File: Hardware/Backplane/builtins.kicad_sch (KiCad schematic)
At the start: 37 parts, among them J1003 BM04B-SRSS-TB, J1004 BM04B-SRSS-TB, J1005 BM04B-SRSS-TB, J1006 BM04B-SRSS-TB, Q1004 S3134K, Q1005 S3134K, SW1001 Button 12mm, U1003 CD74HC221M96, U1004 PCF8523T/1,118, Y1001 32.768k

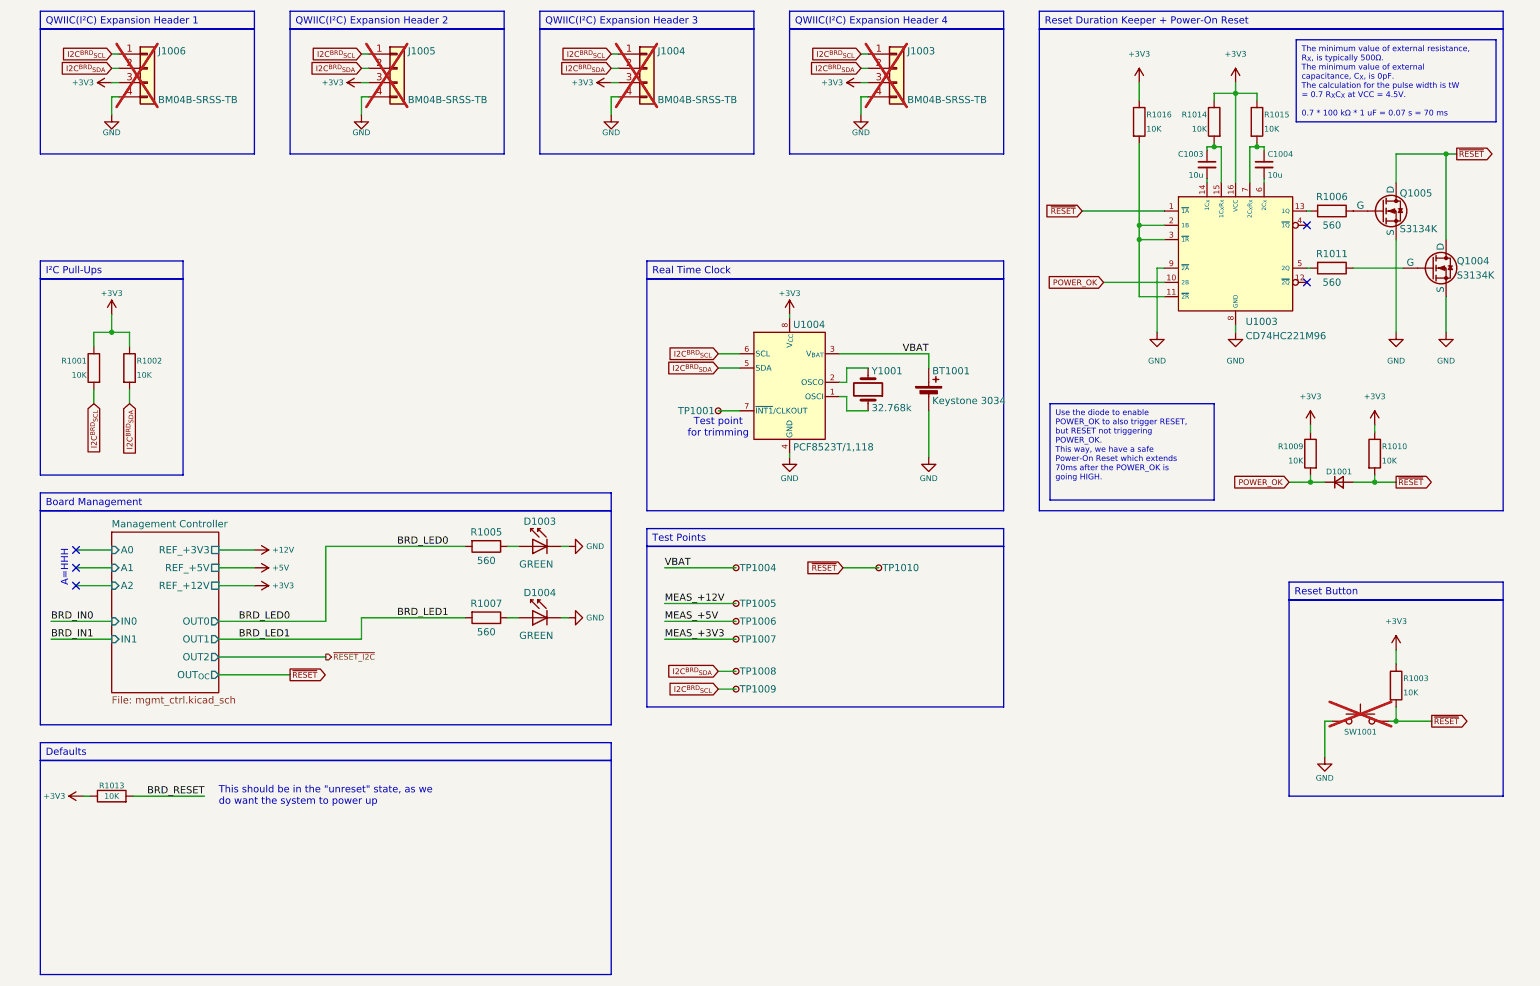
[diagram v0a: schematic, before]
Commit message: Fixes several issues with the backplane schematic.
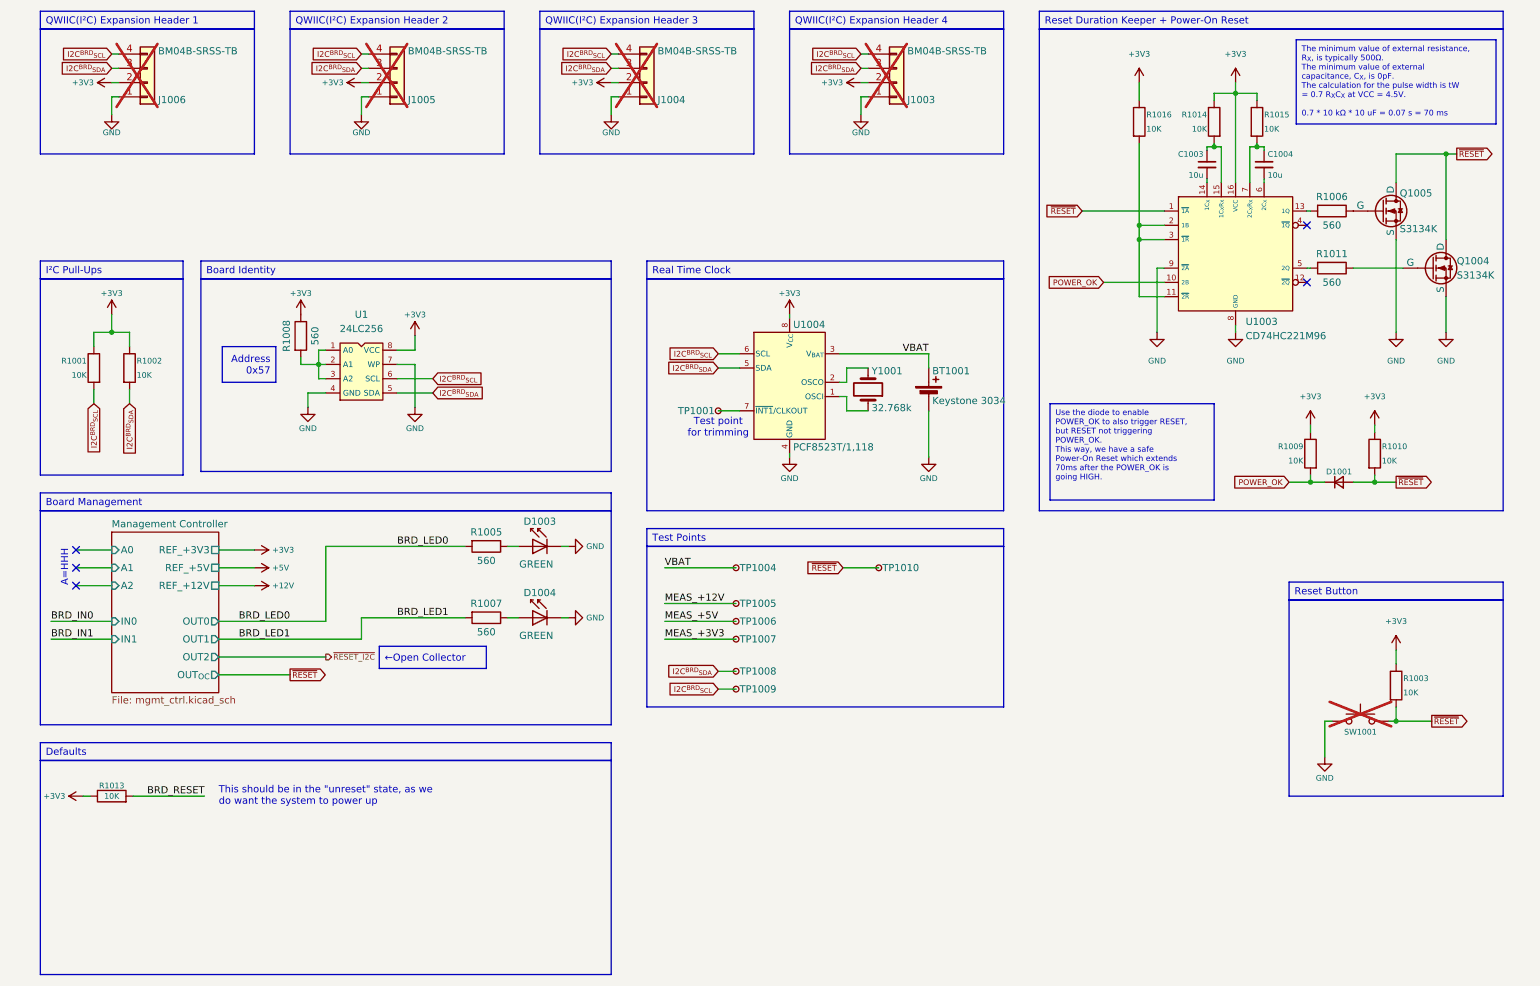
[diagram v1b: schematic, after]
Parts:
- added R1008: 560, Resistor_SMD:R_0603_1608Metric, symbol Device:R
- added U1: 24LC256, Package_SO:SOIC-8_3.9x4.9mm_P1.27mm, symbol Home Computer:24LC256
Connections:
- net +3V3: now also J1003.2 (Pin_2), J1004.2 (Pin_2), J1005.2 (Pin_2), J1006.2 (Pin_2), R1008.1, U1.8 (VCC); no longer J1003.3 (Pin_3), J1004.3 (Pin_3), J1005.3 (Pin_3), J1006.3 (Pin_3)
- net GND: now also J1003.1 (Pin_1), J1004.1 (Pin_1), J1005.1 (Pin_1), J1006.1 (Pin_1), U1.4 (GND), U1.7 (WP); no longer J1003.4 (Pin_4), J1004.4 (Pin_4), J1005.4 (Pin_4), J1006.4 (Pin_4)
- net I2C^{BRD}_{SCL}: now also J1003.4 (Pin_4), J1004.4 (Pin_4), J1005.4 (Pin_4), J1006.4 (Pin_4), U1.6 (SCL); no longer J1003.1 (Pin_1), J1004.1 (Pin_1), J1005.1 (Pin_1), J1006.1 (Pin_1)
- net I2C^{BRD}_{SDA}: now also J1003.3 (Pin_3), J1004.3 (Pin_3), J1005.3 (Pin_3), J1006.3 (Pin_3), U1.5 (SDA); no longer J1003.2 (Pin_2), J1004.2 (Pin_2), J1005.2 (Pin_2), J1006.2 (Pin_2)
- new net: R1008.2, U1.1 (A0), U1.2 (A1), U1.3 (A2)

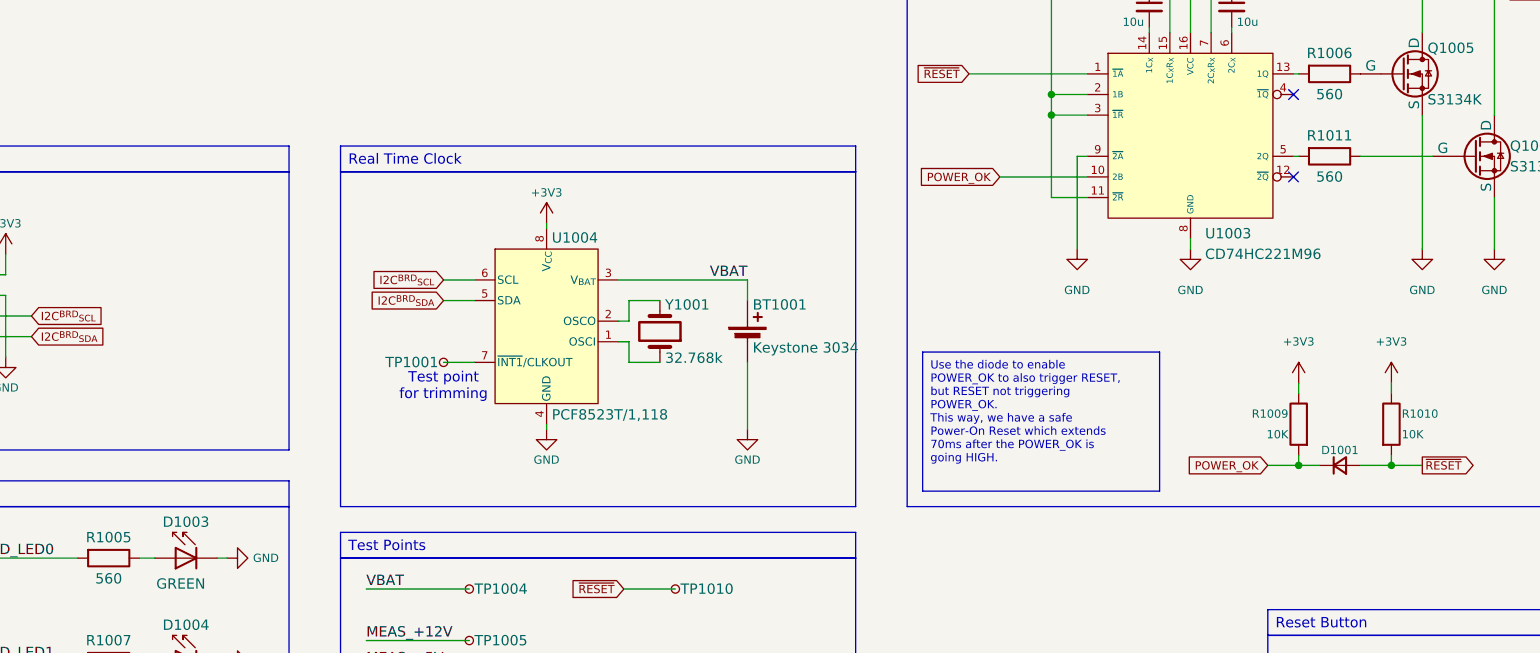
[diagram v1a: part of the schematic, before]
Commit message: Updates the backplane to fit the new platform definition, replaces now deprecated RTC with a new one, improves power management.
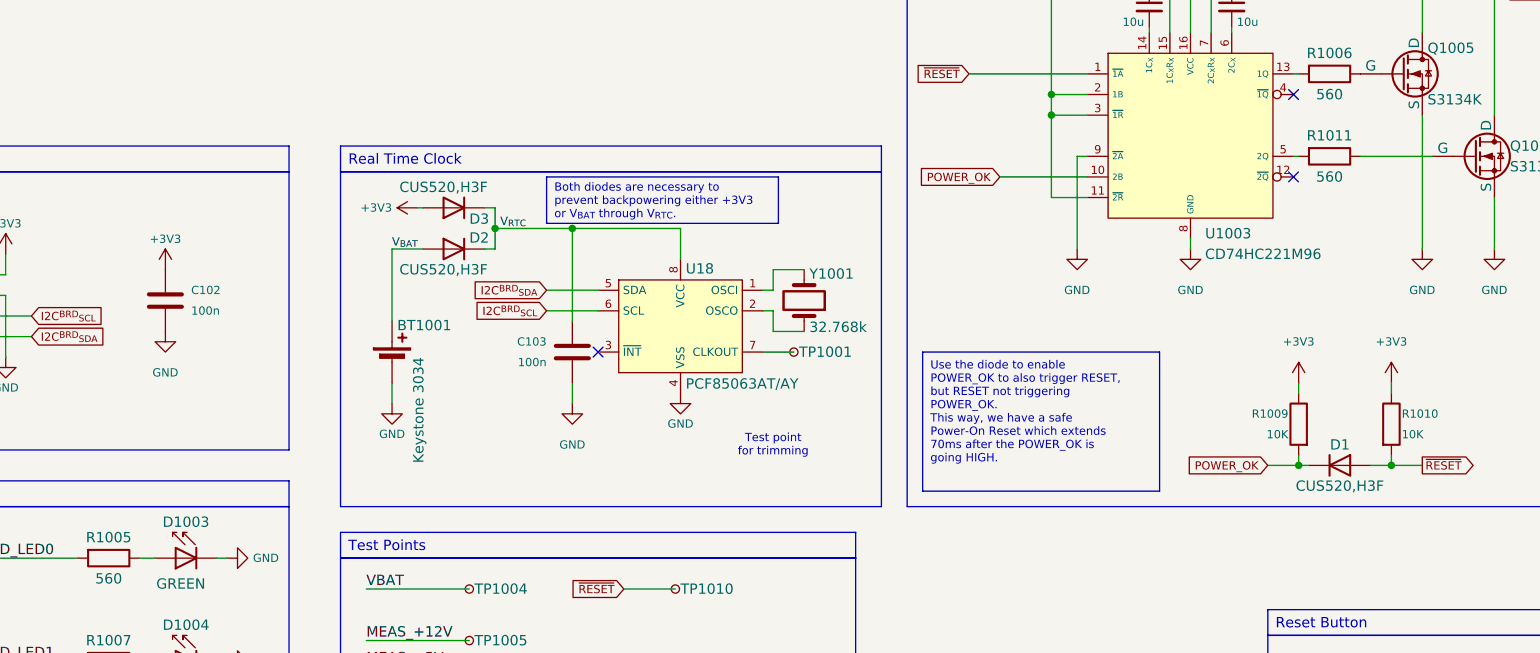
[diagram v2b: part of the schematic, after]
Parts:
- removed D1001: Something Short-Circuit Safe, Diode_SMD:D_1206_3216Metric, symbol Device:D_Small
- removed U1004: PCF8523T/1,118, Home Computer:PCF8523T1,118, symbol Home Computer:PCF8523T/1
- added C102, C103: 100n, Capacitor_SMD:C_0603_1608Metric, symbol Device:C
- added D1, D2, D3: CUS520,H3F, Diode_SMD:D_SOD-323_HandSoldering, symbol Home Computer:CUS520,H3F
- added U18: PCF85063AT/AY, Package_SO:SO-8_3.9x4.9mm_P1.27mm, symbol Home Computer:PCF85063AT/AY
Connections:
- net +3V3: now also C102.2, D3.2 (A)
- net GND: now also C102.1, C103.1, U18.4 (VSS)
- net I2C^{BRD}_{SCL}: now also U18.6 (SCL)
- net I2C^{BRD}_{SDA}: now also U18.5 (SDA)
- net POWER_OK: now also D1.1 (K)
- net VBAT: no longer BT1001.1 (+)
- net ~{RESET}: now also D1.2 (A)
- net at Y1001.1: now also U18.2 (OSCO)
- net at Y1001.2: now also U18.1 (OSCI)
- net at TP1001.1: now also U18.7 (CLKOUT)
- new net V_{BAT}: BT1001.1 (+), D2.2 (A)
- new net V_{RTC}: C103.2, D2.1 (K), D3.1 (K), U18.8 (VCC)
- no-connect marks 5 -> 6
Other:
- moved on the sheet: BT1001, TP1001, Y1001

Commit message: Improves backplane schematic even more
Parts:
- removed D1: CUS520,H3F, Diode_SMD:D_SOD-323_HandSoldering, symbol Home Computer:CUS520,H3F
- removed R1009, R1010, R1013: 10K, Resistor_SMD:R_0603_1608Metric, symbol Device:R
- removed TP1006, TP1007: TestPoint_Small, TestPoint:TestPoint_Pad_D1.0mm, symbol Connector:TestPoint_Small
- added C134, C135: 100n, Capacitor_SMD:C_0603_1608Metric, symbol Device:C
- added U45: NL7SZ57DBVT1G, Package_TO_SOT_SMD:SC-74-6_1.55x2.9mm_P0.95mm, symbol Home Computer:NL7SZ57DBVT1G
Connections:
- net MEAS_+12V is gone; now on net V_{RTC}: TP1005.1
- net VBAT is gone; now on net V_{BAT}: TP1004.1
- net +3V3: now also C134.2, C135.2, U45.5 (VCC)
- net GND: now also C134.1, C135.1, U45.2 (GND)
- net POWER_OK: now also U45.3 (A), U45.6 (C)
- net at R1011.2: now also U45.4 (Y); no longer U1003.5 (2Q)
- new net POWER_OK_{posedge}: U1003.5 (2Q), U45.1 (B)
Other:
- note removed: "This should be in the "unreset" state, as we do want the system to power up"
- moved on the sheet: Q1004, Q1005, R1003, R1006, R1011, SW1001, TP1005
